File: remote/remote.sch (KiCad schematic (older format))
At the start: 37 parts, among them SW1 SW_Push, U1 STM32F030F4Px, U2 RFM69CW-915MHZ

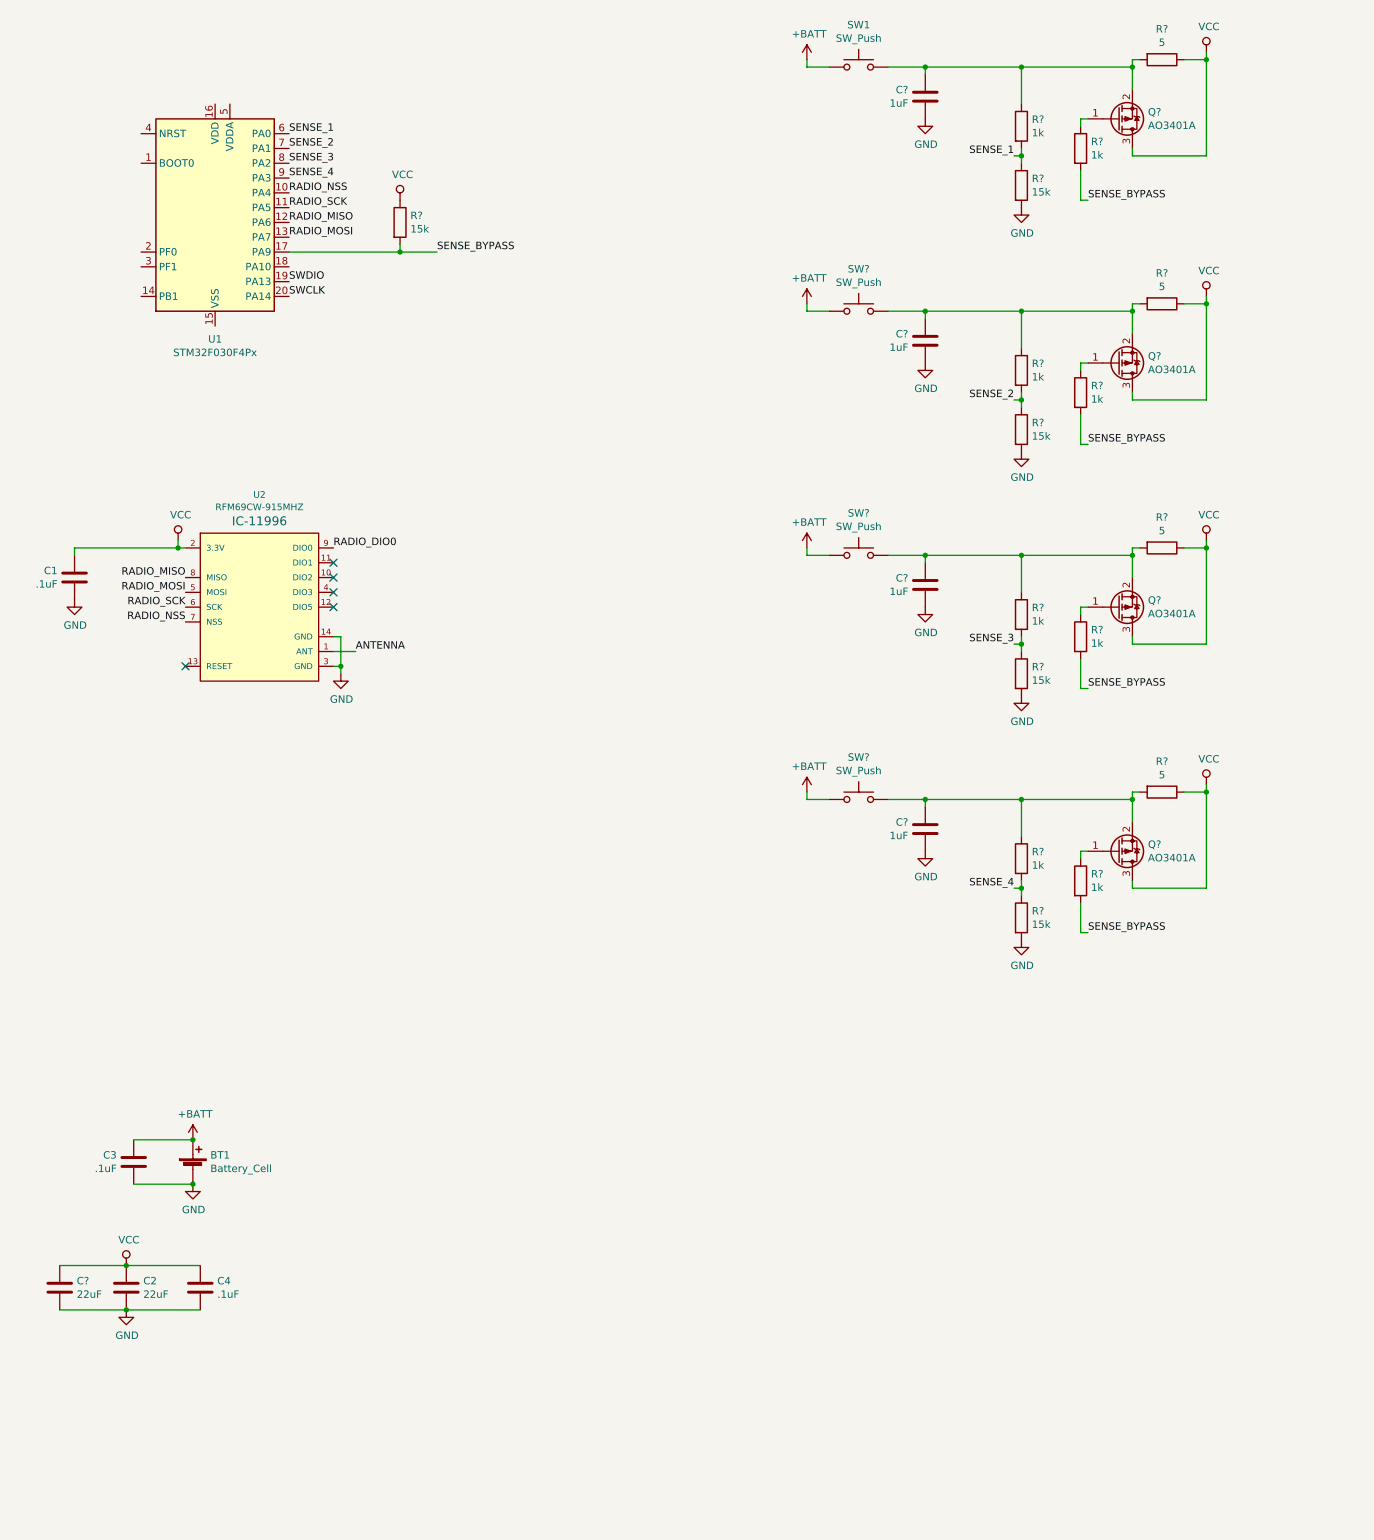
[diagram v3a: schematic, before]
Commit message: Schematic and footprint associations completed for first pass
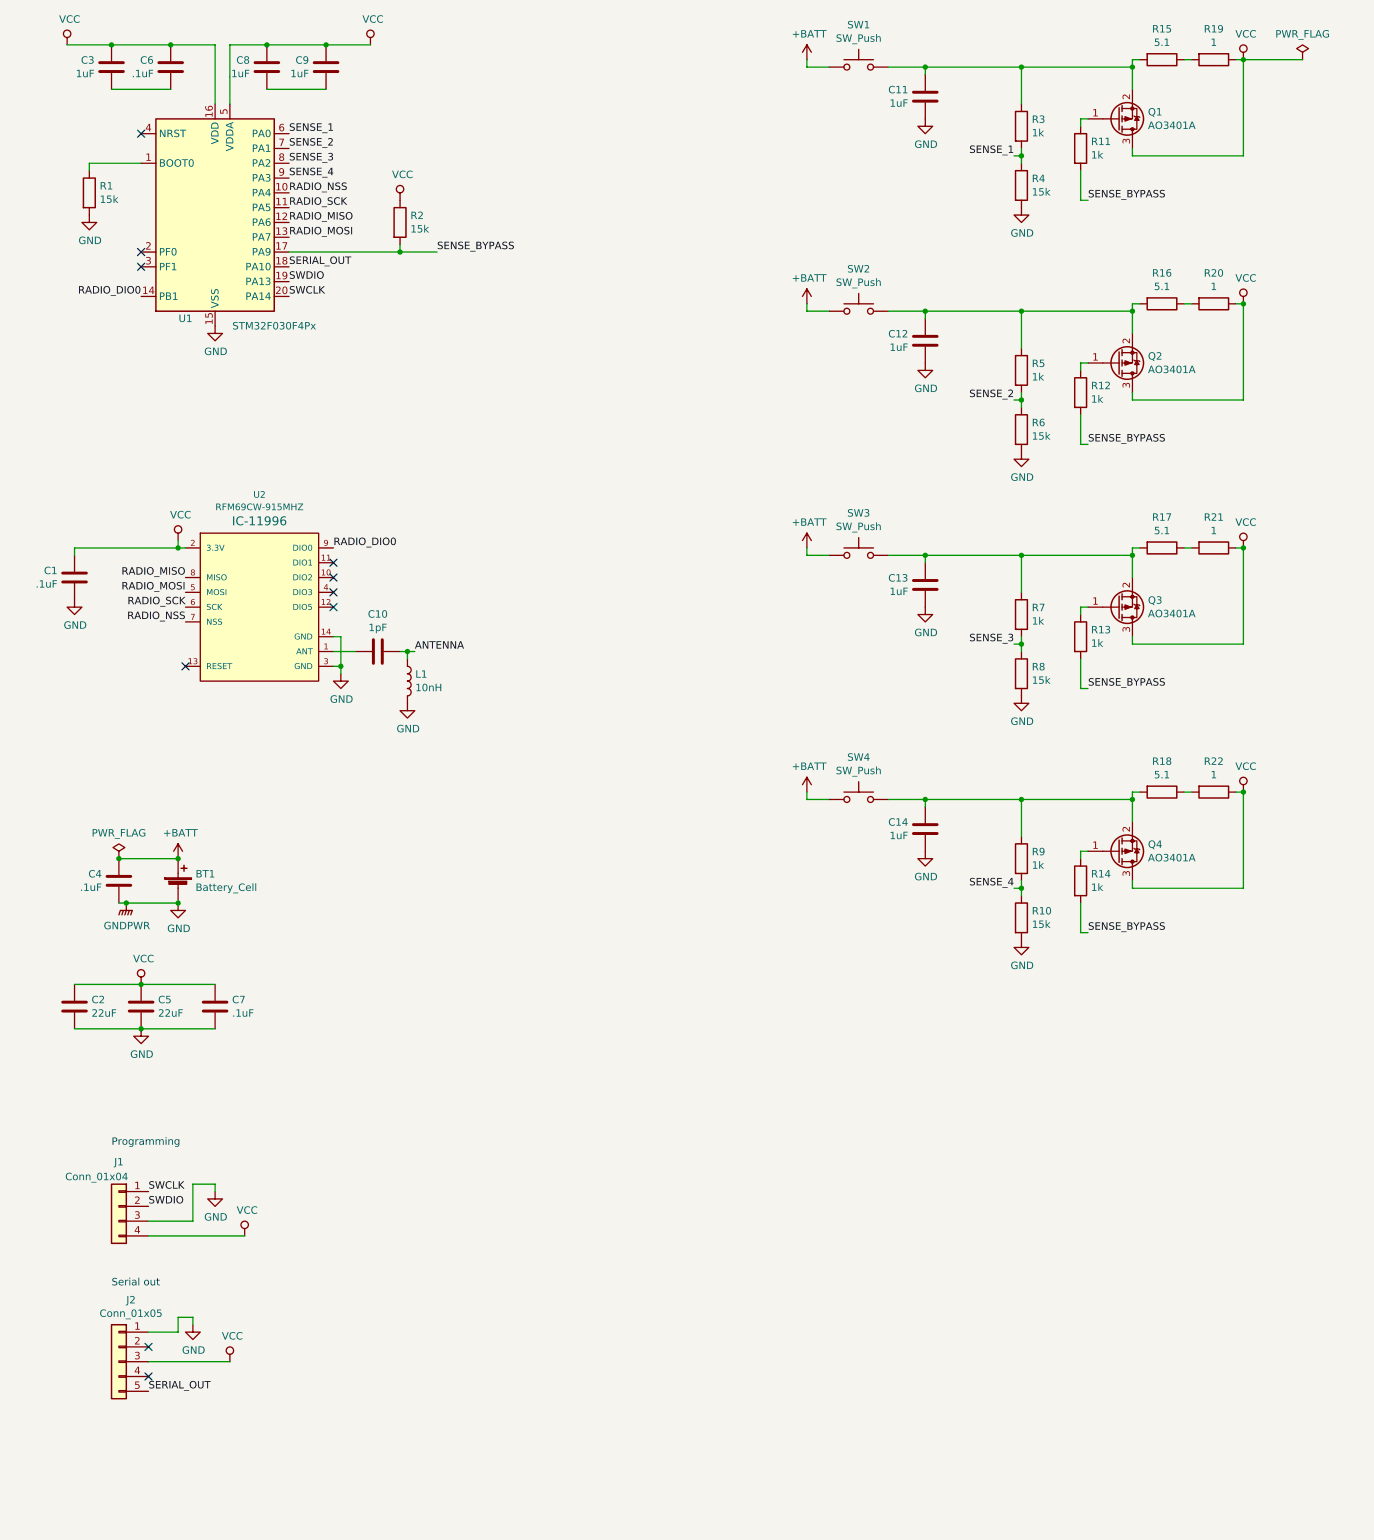
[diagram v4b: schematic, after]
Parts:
- removed C2: 22uF, symbol Device:C
- removed C? (x4): 1uF, symbol Device:C
- removed Q? (x3): AO3401A, Package_TO_SOT_SMD:SOT-23, symbol Transistor_FET:AO3401A
- removed R? (x7): 1k, symbol Device:R
- removed R? (x5): 15k, symbol Device:R
- removed R? (x3): 5, symbol Device:R
- removed SW? (x3): SW_Push, symbol Switch:SW_Push
- added C10: 1pF, Capacitor_SMD:C_0402_1005Metric, symbol Device:C
- added C11, C12, C13, C14, C9: 1uF, Capacitor_SMD:C_0402_1005Metric, symbol Device:C
- added C5: 22uF, Capacitor_SMD:C_0603_1608Metric, symbol Device:C
- added C6, C7, C8: .1uF, Capacitor_SMD:C_0402_1005Metric, symbol Device:C
- added J1: Conn_01x04, Connector_PinSocket_2.54mm:PinSocket_1x04_P2.54mm_Vertical, symbol Connector_Generic:Conn_01x04
- added J2: Conn_01x05, Connector_PinSocket_2.54mm:PinSocket_1x05_P2.54mm_Vertical, symbol Connector_Generic:Conn_01x05
- added L1: 10nH, Inductor_SMD:L_0603_1608Metric, symbol Device:L
- added Q2, Q3, Q4: AO3401A, Package_TO_SOT_SMD:SOT-23, symbol Transistor_FET:AO3401A
- added R1, R10, R2, R4, R6, R8: 15k, Resistor_SMD:R_0402_1005Metric, symbol Device:R
- added R11, R12, R13, R14, R5, R7, R9: 1k, Resistor_SMD:R_0402_1005Metric, symbol Device:R
- added R16, R17, R18: 5.1, Resistor_SMD:R_0603_1608Metric, symbol Device:R
- added R19, R20, R21, R22: 1, Resistor_SMD:R_0402_1005Metric, symbol Device:R
- added SW2, SW3, SW4: SW_Push, homebrew:SW_TACTILE_5.1MM_TS-1187A-C-D-B, symbol Switch:SW_Push
- BT1: footprint (none) -> Battery:BatteryHolder_Keystone_3008_1x2450
- C1, C4: footprint (none) -> Capacitor_SMD:C_0402_1005Metric; LCSC (none) -> C1525
- C2: renamed from C?; footprint (none) -> Capacitor_SMD:C_0603_1608Metric; LCSC (none) -> C59461
- C3: value .1uF -> 1uF; footprint (none) -> Capacitor_SMD:C_0402_1005Metric; LCSC (none) -> C52923
- Q1: renamed from Q?; LCSC (none) -> C15127
- R15: renamed from R?; value 5 -> 5.1; footprint (none) -> Resistor_SMD:R_0603_1608Metric; LCSC (none) -> C25197
- R3: renamed from R?; footprint (none) -> Resistor_SMD:R_0402_1005Metric; LCSC (none) -> C11702
- SW1: footprint (none) -> homebrew:SW_TACTILE_5.1MM_TS-1187A-C-D-B; LCSC (none) -> C318888
- U2: footprint RFM69CW-XXXS2 -> homebrew:RFM69CW-minimalpads
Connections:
- net +BATT: now also C4.2, SW2.1, SW3.1, SW4.1; no longer C3.2
- net ANTENNA: now also C10.1, L1.1; no longer U2.1 (ANT)
- net GND: now also U1.15 (VSS), C11.1, C12.1, C13.1, C14.1, C5.2, C7.1, J1.3 (Pin_3), J2.1 (Pin_1), L1.2, R1.2, R10.2, R4.2, R6.2, R8.2; no longer C3.1
- net RADIO_DIO0: now also U1.14 (PB1)
- net SENSE_1: now also R4.1
- net SENSE_2: now also R5.2, R6.1
- net SENSE_3: now also R7.2, R8.1
- net SENSE_4: now also R10.1, R9.2
- net SENSE_BYPASS: now also R11.2, R12.2, R13.2, R14.2, R2.2
- net SWCLK: now also J1.1 (Pin_1)
- net SWDIO: now also J1.2 (Pin_2)
- net VCC: now also C3.2, U1.16 (VDD), U1.5 (VDDA), C5.1, C6.2, C7.2, C8.2, C9.2, J1.4 (Pin_4), J2.3 (Pin_3), Q2.3 (D), Q3.3 (D), Q4.3 (D), R19.1, R2.1, R20.1, R21.1, R22.1; no longer C4.2, R15.1
- net at U1.1 (BOOT0): now also R1.1
- net SERIAL_OUT: now reaches U1.18 (PA10)
- net SERIAL_OUT: now also J2.5 (Pin_5)
- net at Q1.2 (S), R15.2, R3.1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: now also C11.2
- net at Q1.1 (G): now also R11.1
- new net: C10.2, U2.1 (ANT)
- new net: R15.1, R19.2
- new net: C3.1, C6.1
- new net: C8.1, C9.1
- new net: C12.2, Q2.2 (S), R16.2, R5.1, SW2.2
- new net: Q2.1 (G), R12.1
- new net: R16.1, R20.2
- new net: C13.2, Q3.2 (S), R17.2, R7.1, SW3.2
- new net: Q3.1 (G), R13.1
- new net: R17.1, R21.2
- new net: C14.2, Q4.2 (S), R18.2, R9.1, SW4.2
- new net: Q4.1 (G), R14.1
- new net: R18.1, R22.2
- no-connect marks 5 -> 10
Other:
- note added: "Programming"
- note added: "Serial out"
- moved on the sheet: BT1, C2

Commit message: Start layout - outline and easy placement
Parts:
- added D1: LED, LED_SMD:LED_0603_1608Metric, symbol Device:LED
- added H1, H2, H3, H4: HOLE, MountingHole:MountingHole_4.3mm_M4_ISO14580, symbol Homebrew:HOLE
- added R23: 680k, Resistor_SMD:R_0603_1608Metric, symbol Device:R
- C10: footprint Capacitor_SMD:C_0402_1005Metric -> Capacitor_SMD:C_0603_1608Metric_Pad1.05x0.95mm_HandSolder; LCSC C1550 -> (none); Part (none) -> VJ0603A1R0BXACW1BC‎
- L1: footprint Inductor_SMD:L_0603_1608Metric -> Inductor_SMD:L_0603_1608Metric_Pad1.05x0.95mm_HandSolder; LCSC C15666 -> (none); Part (none) -> BWCS0016100810NG00
- R10, R6, R8: value 15k -> 47k; LCSC C25756 -> C25792
- R19, R20, R21, R22: value 1 -> 0; LCSC C25086 -> C17168
- R3: value 1k -> 47k; LCSC C11702 -> C25792
- R4: value 15k -> 680k; footprint Resistor_SMD:R_0402_1005Metric -> Resistor_SMD:R_0603_1608Metric; LCSC C25756 -> C25822
- R7, R9: value 1k -> 680k; footprint Resistor_SMD:R_0402_1005Metric -> Resistor_SMD:R_0603_1608Metric; LCSC C11702 -> C25822
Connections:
- net GND: now also R5.2, R7.2, R9.2, R23.2; no longer R10.2, R6.2, R8.2
- net SENSE_2: now also R6.2, R7.1; no longer R5.2, R6.1
- net SENSE_3: now also R8.2, R9.1; no longer R7.2, R8.1
- net SENSE_4: now also R10.2, R23.1; no longer R10.1, R9.2
- net SERIAL_OUT: now also D1.2 (A)
- net at C12.2, Q2.2 (S), R16.2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: now also R6.1; no longer R5.1
- net at C13.2, Q3.2 (S), R17.2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: now also R8.1; no longer R7.1
- net at C14.2, Q4.2 (S), R18.2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: now also R10.1; no longer R9.1
- new net: D1.1 (K), R5.1

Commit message: Start laying out - antenna and power
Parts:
- added C15: .1uF, Capacitor_SMD:C_0402_1005Metric, symbol Device:C
- H1, H2, H3, H4: symbol Homebrew:HOLE -> remote-rescue:HOLE-Homebrew
- R19, R20, R21, R22: footprint Resistor_SMD:R_0402_1005Metric -> Resistor_SMD:R_0603_1608Metric_Pad1.05x0.95mm_HandSolder; LCSC C17168 -> C21189
- U2: symbol SparkFun-RF:RFM69CW-915MHZ -> remote-rescue:RFM69CW-915MHZ-SparkFun-RF
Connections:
- net +BATT: now also C15.2
- net GND: now also C3.1, C6.1, C8.1, C9.1, C15.1
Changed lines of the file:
@@
 $EndComp
 $Comp
-L SparkFun-RF:RFM69CW-915MHZ U2
+L remote-rescue:RFM69CW-915MHZ-SparkFun-RF U2
 U 1 1 5F813DE5
 P 2200 4550
@@
 F 0 "R19" V 8443 850 50  0000 C CNN
 F 1 "0" V 8534 850 50  0000 C CNN
-F 2 "Resistor_SMD:R_0402_1005Metric" V 8580 850 50  0001 C CNN
+F 2 "Resistor_SMD:R_0603_1608Metric_Pad1.05x0.95mm_HandSolder" V 8580 850 50  0001 C CNN
 F 3 "~" H 8650 850 50  0001 C CNN
-F 4 "C17168" V 8650 850 50  0001 C CNN "LCSC"
+F 4 "C21189" V 8650 850 50  0001 C CNN "LCSC"
 	1    8650 850
 	0    1    1    0
@@
 Connection ~ 1500 9850
 $Comp
-L Device:R R20
-U 1 1 5F8739BA
-P 8650 2500
-F 0 "R20" V 8443 2500 50  0000 C CNN
-F 1 "0" V 8534 2500 50  0000 C CNN
-F 2 "Resistor_SMD:R_0402_1005Metric" V 8580 2500 50  0001 C CNN
-F 3 "~" H 8650 2500 50  0001 C CNN
-F 4 "C17168" V 8650 2500 50  0001 C CNN "LCSC"
-	1    8650 2500
-	0    1    1    0
-$EndComp
-$Comp
-L Device:R R21
-U 1 1 5F8740A5
-P 8650 4150
-F 0 "R21" V 8443 4150 50  0000 C CNN
-F 1 "0" V 8534 4150 50  0000 C CNN
-F 2 "Resistor_SMD:R_0402_1005Metric" V 8580 4150 50  0001 C CNN
-F 3 "~" H 8650 4150 50  0001 C CNN
-F 4 "C17168" V 8650 4150 50  0001 C CNN "LCSC"
-	1    8650 4150
-	0    1    1    0
-$EndComp
-$Comp
-L Device:R R22
-U 1 1 5F87476A
-P 8650 5800
-F 0 "R22" V 8443 5800 50  0000 C CNN
-F 1 "0" V 8534 5800 50  0000 C CNN
-F 2 "Resistor_SMD:R_0402_1005Metric" V 8580 5800 50  0001 C CNN
-F 3 "~" H 8650 5800 50  0001 C CNN
-F 4 "C17168" V 8650 5800 50  0001 C CNN "LCSC"
-	1    8650 5800
-	0    1    1    0
-$EndComp
-$Comp
-L Homebrew:HOLE H1
+L remote-rescue:HOLE-Homebrew H1
 U 1 1 5F887DE3
 P 3500 8000
@@
 $EndComp
 $Comp
-L Homebrew:HOLE H2
+L remote-rescue:HOLE-Homebrew H2
 U 1 1 5F888618
 P 3500 8200
@@
 $EndComp
 $Comp
-L Homebrew:HOLE H3
+L remote-rescue:HOLE-Homebrew H3
 U 1 1 5F8888BC
 P 3500 8400
@@
 $EndComp
 $Comp
-L Homebrew:HOLE H4
+L remote-rescue:HOLE-Homebrew H4
 U 1 1 5F888B68
 P 3500 8600
@@
 	1    0    0    -1
 $EndComp
+$Comp
+L power:GND #PWR0101
+U 1 1 5F8651D3
+P 1200 1050
+F 0 "#PWR0101" H 1200 800 50  0001 C CNN
+F 1 "GND" H 1205 877 50  0000 C CNN
+F 2 "" H 1200 1050 50  0001 C CNN
+F 3 "" H 1200 1050 50  0001 C CNN
+	1    1200 1050
+	1    0    0    -1
+$EndComp
+Connection ~ 2650 1050
+$Comp
+L power:GND #PWR0102
+U 1 1 5F865AF9
+P 2650 1050
+F 0 "#PWR0102" H 2650 800 50  0001 C CNN
+F 1 "GND" H 2655 877 50  0000 C CNN
+F 2 "" H 2650 1050 50  0001 C CNN
+F 3 "" H 2650 1050 50  0001 C CNN
+	1    2650 1050
+	1    0    0    -1
+$EndComp
+Connection ~ 1200 1050
+$Comp
+L Device:C C15
+U 1 1 5F86F083
+P 850 6400
+F 0 "C15" H 735 6354 50  0000 R CNN
+F 1 ".1uF" H 735 6445 50  0000 R CNN
+F 2 "Capacitor_SMD:C_0402_1005Metric" H 888 6250 50  0001 C CNN
+F 3 "~" H 850 6400 50  0001 C CNN
+F 4 "C1525" H 850 6400 50  0001 C CNN "LCSC"
+	1    850  6400
+	1    0    0    1
+$EndComp
+Wire Wire Line
+	850  6250 1250 6250
+Wire Wire Line
+	1250 6550 850  6550
+Connection ~ 1250 6550
+$Comp
+L Device:R R20
+U 1 1 5F87D1A4
+P 8650 2500
+F 0 "R20" V 8443 2500 50  0000 C CNN
+F 1 "0" V 8534 2500 50  0000 C CNN
+F 2 "Resistor_SMD:R_0603_1608Metric_Pad1.05x0.95mm_HandSolder" V 8580 2500 50  0001 C CNN
+F 3 "~" H 8650 2500 50  0001 C CNN
+F 4 "C21189" V 8650 2500 50  0001 C CNN "LCSC"
+	1    8650 2500
+	0    1    1    0
+$EndComp
+$Comp
+L Device:R R21
+U 1 1 5F87DB75
+P 8650 4150
+F 0 "R21" V 8443 4150 50  0000 C CNN
+F 1 "0" V 8534 4150 50  0000 C CNN
+F 2 "Resistor_SMD:R_0603_1608Metric_Pad1.05x0.95mm_HandSolder" V 8580 4150 50  0001 C CNN
+F 3 "~" H 8650 4150 50  0001 C CNN
+F 4 "C21189" V 8650 4150 50  0001 C CNN "LCSC"
+	1    8650 4150
+	0    1    1    0
+$EndComp
+$Comp
+L Device:R R22
+U 1 1 5F8805EC
+P 8650 5800
+F 0 "R22" V 8443 5800 50  0000 C CNN
+F 1 "0" V 8534 5800 50  0000 C CNN
+F 2 "Resistor_SMD:R_0603_1608Metric_Pad1.05x0.95mm_HandSolder" V 8580 5800 50  0001 C CNN
+F 3 "~" H 8650 5800 50  0001 C CNN
+F 4 "C21189" V 8650 5800 50  0001 C CNN "LCSC"
+	1    8650 5800
+	0    1    1    0
+$EndComp
 $EndSCHEMATC

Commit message: Finish remote v1.0
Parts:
- U1: LCSC (none) -> C89040
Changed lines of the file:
@@
 F 2 "Package_SO:TSSOP-20_4.4x6.5mm_P0.65mm" H 1500 1150 50  0001 R CNN
 F 3 "http://www.st.com/st-web-ui/static/active/en/resource/technical/document/datasheet/DM00088500.pdf" H 1900 1850 50  0001 C CNN
+F 4 "C89040" H 1900 1850 50  0001 C CNN "LCSC"
 	1    1900 1850
 	1    0    0    -1
